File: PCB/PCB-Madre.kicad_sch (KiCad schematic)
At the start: 4 parts

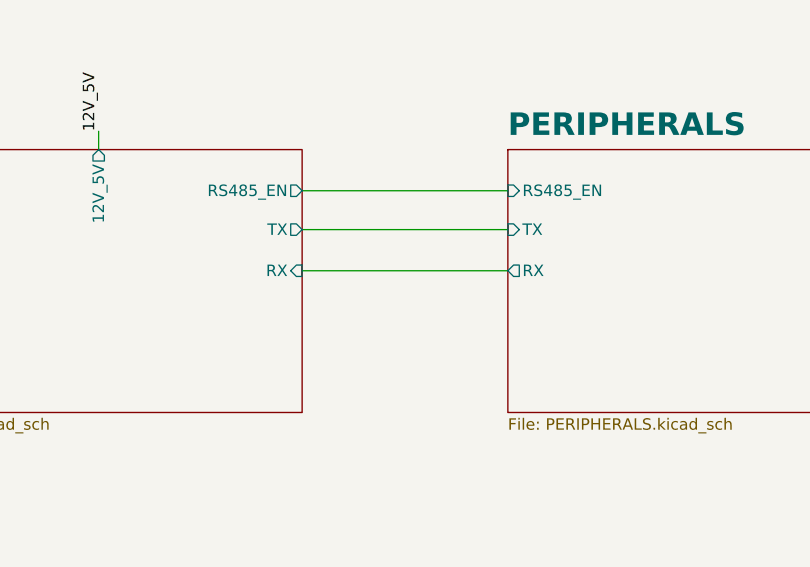
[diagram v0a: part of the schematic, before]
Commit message: pcb board terminada
Se termino:
- PCB board
- Labels de conectores y logo de la empresa
- Conexion WIZ850IO
- Conexion de MCU y WIZ850IO
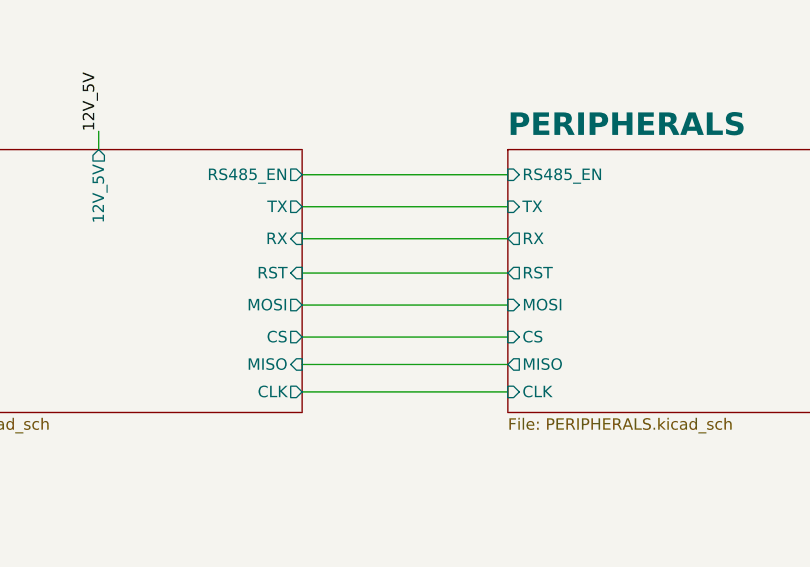
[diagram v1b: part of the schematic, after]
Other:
- sheet MCU ports: added CLK, CS, MISO, MOSI, RST; removed none
- sheet PERIPHERALS ports: added CLK, CS, MISO, MOSI, RST; removed none
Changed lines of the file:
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@@
+	(wire
+		(pts
+			(xy 177.8 91.694) (xy 200.66 91.694)
+		)
+		(stroke
+			(width 0)
+			(type default)
+		)
+	)
+	(wire
+		(pts
+			(xy 177.8 88.138) (xy 200.66 88.138)
+		)
+		(stroke
+			(width 0)
+			(type default)
+		)
+	)
 	(wire
 		(pts
@@
 	(wire
 		(pts
-			(xy 177.8 87.884) (xy 200.66 87.884)
+			(xy 177.8 84.328) (xy 200.66 84.328)
 		)
 		(stroke
@@
 	(wire
 		(pts
-			(xy 177.8 78.994) (xy 200.66 78.994)
-		)
-		(stroke
-			(width 0)
-			(type default)
-		)
-	)
-	(wire
-		(pts
-			(xy 177.8 83.312) (xy 200.66 83.312)
+			(xy 177.8 77.216) (xy 200.66 77.216)
+		)
+		(stroke
+			(width 0)
+			(type default)
+		)
+	)
+	(wire
+		(pts
+			(xy 177.8 95.25) (xy 200.66 95.25)
+		)
+		(stroke
+			(width 0)
+			(type default)
+		)
+	)
+	(wire
+		(pts
+			(xy 177.8 98.298) (xy 200.66 98.298)
+		)
+		(stroke
+			(width 0)
+			(type default)
+		)
+	)
+	(wire
+		(pts
+			(xy 177.8 101.346) (xy 200.66 101.346)
+		)
+		(stroke
+			(width 0)
+			(type default)
+		)
+	)
+	(wire
+		(pts
+			(xy 177.8 80.772) (xy 200.66 80.772)
 		)
 		(stroke
@@
 		)
 		(pin "RX" input
-			(at 177.8 87.884 0)
+			(at 177.8 84.328 0)
 			(effects
 				(font
@@
 		)
 		(pin "TX" output
-			(at 177.8 83.312 0)
+			(at 177.8 80.772 0)
 			(effects
 				(font
@@
 		)
 		(pin "RS485_EN" output
-			(at 177.8 78.994 0)
+			(at 177.8 77.216 0)
 			(effects
 				(font
@@
 		(pin "12V_5V" output
 			(at 155.194 74.422 90)
+			(effects
+				(font
+					(size 1.27 1.27)
+				)
+				(justify right)
+			)
+		)
+		(pin "RST" input
+			(at 177.8 88.138 0)
+			(effects
+				(font
+					(size 1.27 1.27)
+				)
+				(justify right)
+			)
+		)
+		(pin "MOSI" output
+			(at 177.8 91.694 0)
+			(effects
+				(font
+					(size 1.27 1.27)
+				)
+				(justify right)
+			)
+		)
+		(pin "CS" output
+			(at 177.8 95.25 0)
+			(effects
+				(font
+					(size 1.27 1.27)
+				)
+				(justify right)
+			)
+		)
+		(pin "MISO" input
+			(at 177.8 98.298 0)
+			(effects
+				(font
+					(size 1.27 1.27)
+				)
+				(justify right)
+			)
+		)
+		(pin "CLK" output
+			(at 177.8 101.346 0)
 			(effects
 				(font
@@
 		)
 		(pin "RX" output
-			(at 200.66 87.884 180)
+			(at 200.66 84.328 180)
 			(effects
 				(font
@@
 		)
 		(pin "TX" input
-			(at 200.66 83.312 180)
+			(at 200.66 80.772 180)
 			(effects
 				(font
@@
 		)
 		(pin "RS485_EN" input
-			(at 200.66 78.994 180)
-			(effects
-				(font
+			(at 200.66 77.216 180)
+			(effects
+				(font
+					(size 1.27 1.27)
+				)
+				(justify left)
+			)
+		)
+		(pin "MOSI" input
+			(at 200.66 91.694 180)
+			(effects
+				(font
+					(size 1.27 1.27)
+				)
+				(justify left)
+			)
+		)
+		(pin "CLK" input
+			(at 200.66 101.346 180)
+			(effects
+				(font
+					(size 1.27 1.27)
+				)
+				(justify left)
+			)
+		)
+		(pin "CS" input
+			(at 200.66 95.25 180)
+			(effects
+				(font
+					(size 1.27 1.27)
+				)
+				(justify left)
+			)
+		)
+		(pin "MISO" output
+			(at 200.66 98.298 180)
+			(effects
+				(font
+					(size 1.27 1.27)
+				)
+				(justify left)
+			)
+		)
+		(pin "RST" output
+			(at 200.66 88.138 180)
+			(effects
+				(font
